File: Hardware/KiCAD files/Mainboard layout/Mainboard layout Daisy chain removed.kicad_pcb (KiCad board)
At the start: 2 copper layers, 191.3 x 169.2 mm, 88 parts, among them J10 Conn_01x02, J11 Conn_01x04, J12 JST_06, J13 Conn_01x08, J14 Conn_01x08, J15 Screw_Terminal_2_P5.00mm, J17 PINHD_1x8_Male, J18 PINHD_1x8_Male, J19 PINHD_1x8_Male, J2 Screw_Terminal_2_P5.00mm, J20 PINHD_1x8_Male, J22 PINHD_1x8_Male, J23 PINHD_1x8_Male, J24 PINHD_1x8_Male, J25 Conn_01x04, J26 Conn_01x04, J27 Conn_01x04, J28 PINHD_1x8_Male, J3 Screw_Terminal_2_P3.50mm, J30 USB-A1VSB6, J31 JST_03, J32 USB-A1VSB6, J34 JST_03, J35 JST_03, J36 JST_03, J37 JST_03, J38 JST_03, J4 JST_06, J5 Conn_01x04, J6 JST_06, J7 JST_06, J8 Conn_01x06, J9 Conn_01x10, Q1 BS170, Q2 2DD1664, SW1 210-4MS, SW2 210-4MS, SW3 210-4MS, SW4 210-4MS, SW8 Push_Button, SW9 Push_Button, U1 CP2102-GM, U12 ESP32-S3-WROOM-1, U2 PCA9534PW_118, U4 PCA9534PW_118

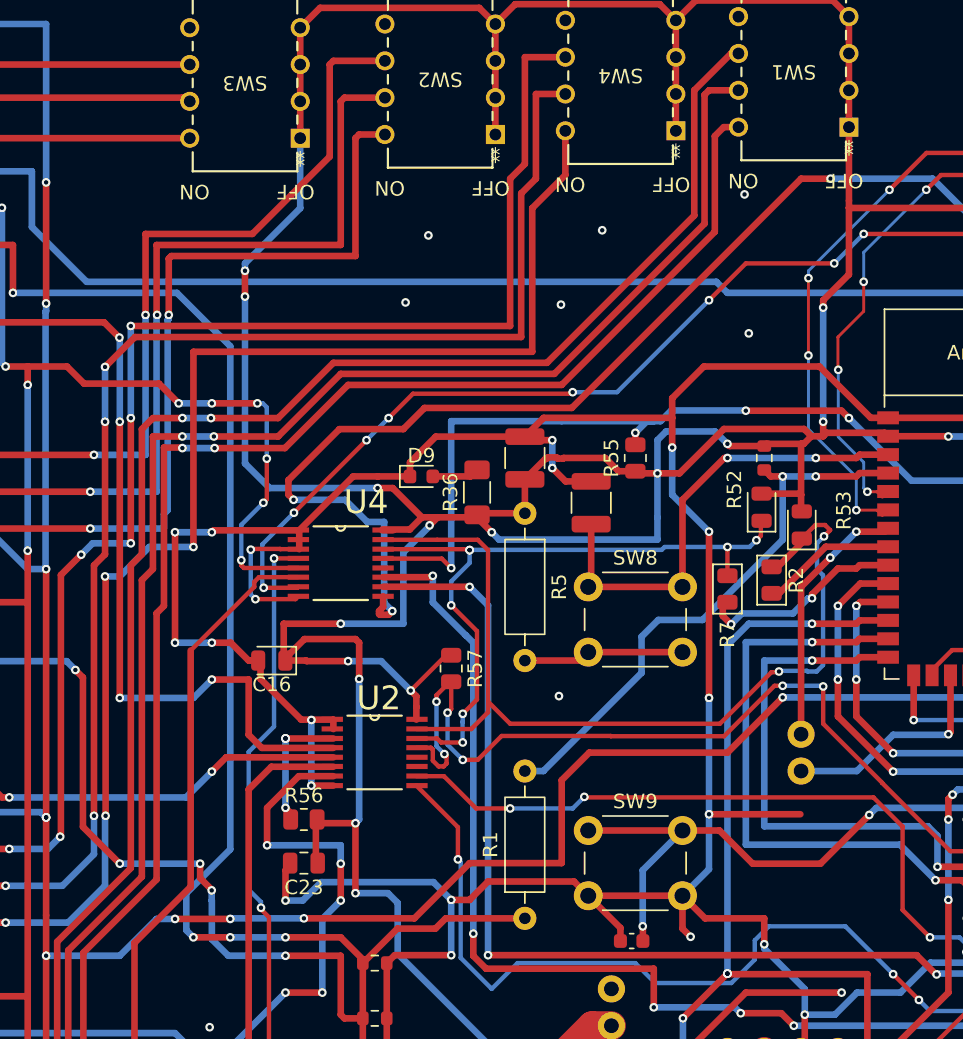
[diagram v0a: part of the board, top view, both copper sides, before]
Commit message: part of the way through next iteration
Non-daisy chain Mainboard is ~50% through
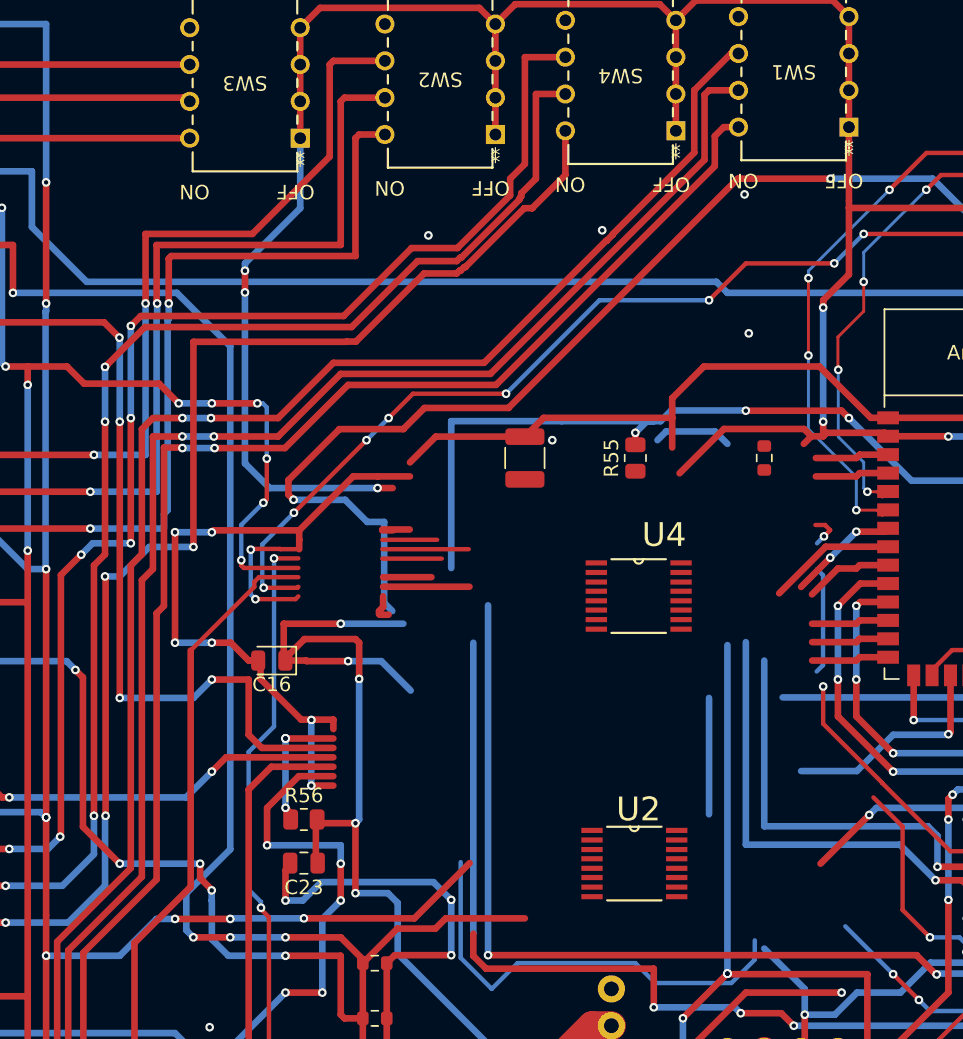
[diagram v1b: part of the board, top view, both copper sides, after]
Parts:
- removed C3: 0.1uF, PCM_SparkFun-Capacitor:C_0603_1608Metric
- removed C4: 10uF, PCM_SparkFun-Capacitor:C_1210_3225Metric
- removed D9: LED, LED_SMD:LED_0603_1608Metric
- removed J10: Conn_01x02, PCM_SparkFun-Connector:1x02_P2.54mm
- removed R1: 1k, Resistor_THT:R_Axial_DIN0207_L6.3mm_D2.5mm_P10.16mm_Horizontal
- removed R2: 50 ohmR_0805, PCM_Resistor_SMD_AKL:R_0805_2012Metric
- removed R36: 1k, Resistor_SMD:R_1206_3216Metric_Pad1.30x1.75mm_HandSolder
- removed R5: 10k, Resistor_THT:R_Axial_DIN0207_L6.3mm_D2.5mm_P10.16mm_Horizontal
- removed R52, R53: 10k, LED_SMD:LED_0805_2012Metric
- removed R57: 10k, Resistor_SMD:R_0805_2012Metric
- removed R7: 50 ohm R_0805, PCM_Resistor_SMD_AKL:R_0805_2012Metric
- removed SW8, SW9: Push_Button, Button_Switch_THT:SW_PUSH_6mm
- moved U4 20.7 mm to (147.6, 36.1)
- moved U2 19.5 mm to (147.2, 54.6)
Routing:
- net +3.3V: track 764.5 -> 691.7 mm, vias 32 -> 27
- net GND: track 1488.8 -> 1417.8 mm, vias 83 -> 74
- net Net-(U2-SDA): track 64.8 -> 13.6 mm, vias 2 -> 1
- net IO_Interupter2: track 96.3 -> 53.8 mm, vias 10 -> 5
- net Net-(U2-SCL): track 47.8 -> 5.97 mm, vias 7 -> 0
- net STEP: track 39.0 -> 5.08 mm, vias 2 -> 0
- net AXIS_Y_ENDSTOP: track 101.4 -> 68.6 mm, vias 6 -> 4
- net N_ENBL: track 223.2 -> 193.5 mm, vias 11 -> 10
- net Net-(U12-EN): track 32.1 -> 5.08 mm, vias 2 -> 0
- net Net-(U12-GPIO0/BOOT): track 62.8 -> 37.1 mm, vias 3 -> 2
- net AXIS_X_ENDSTOP: track 92.0 -> 78.8 mm, vias 5 -> 4
- net Net-(R5-Pad2): track 11.1 -> 0.00 mm
- net Net-(J10-Pin_1): track 17.8 -> 7.67 mm
- net Net-(U12-GPIO16/U0CTS/ADC2_CH5/XTAL_32K_N): track 14.6 -> 6.08 mm, vias 2 -> 0
- net SPI1_CS: track 230.1 -> 223.7 mm, vias 12 -> 11
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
